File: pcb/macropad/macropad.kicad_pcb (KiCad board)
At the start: 2 copper layers, 100 x 100 mm, 21 parts, among them SW1 SW_Push, SW10 RotaryEncoder, SW2 SW_Push, SW3 SW_Push, SW4 SW_Push, SW5 SW_Push, SW6 SW_Push, SW7 SW_Push, SW8 SW_Push, SW9 SW_Push, U1 XIAO-RP2040-DIP

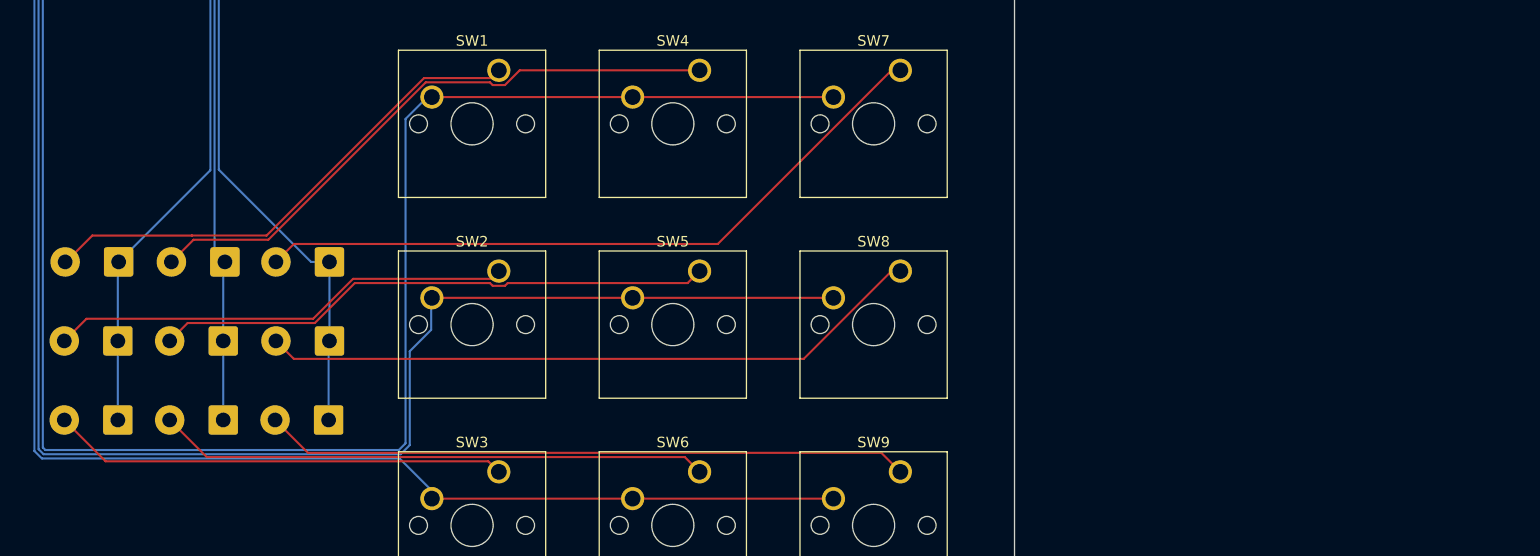
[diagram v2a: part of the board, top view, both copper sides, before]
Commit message: tidy wiring
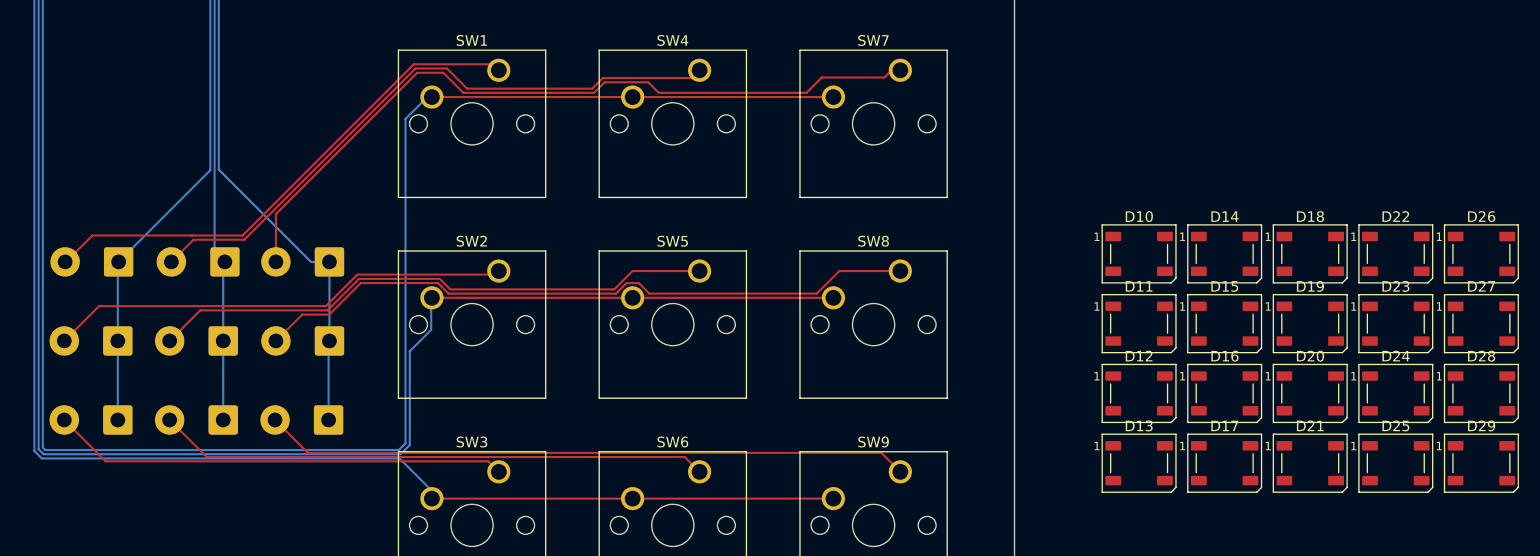
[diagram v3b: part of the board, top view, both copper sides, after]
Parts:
- added D10: WS2812B, LED_SMD:LED_WS2812B_PLCC4_5.0x5.0mm_P3.2mm, F.Cu at (213.8, 104.7)
- added D11: WS2812B, LED_SMD:LED_WS2812B_PLCC4_5.0x5.0mm_P3.2mm, F.Cu at (213.8, 111.4)
- added D12: WS2812B, LED_SMD:LED_WS2812B_PLCC4_5.0x5.0mm_P3.2mm, F.Cu at (213.8, 118.0)
- added D13: WS2812B, LED_SMD:LED_WS2812B_PLCC4_5.0x5.0mm_P3.2mm, F.Cu at (213.8, 124.6)
- added D14: WS2812B, LED_SMD:LED_WS2812B_PLCC4_5.0x5.0mm_P3.2mm, F.Cu at (221.9, 104.7)
- added D15: WS2812B, LED_SMD:LED_WS2812B_PLCC4_5.0x5.0mm_P3.2mm, F.Cu at (221.9, 111.4)
- added D16: WS2812B, LED_SMD:LED_WS2812B_PLCC4_5.0x5.0mm_P3.2mm, F.Cu at (221.9, 118.0)
- added D17: WS2812B, LED_SMD:LED_WS2812B_PLCC4_5.0x5.0mm_P3.2mm, F.Cu at (221.9, 124.6)
- added D18: WS2812B, LED_SMD:LED_WS2812B_PLCC4_5.0x5.0mm_P3.2mm, F.Cu at (230.1, 104.7)
- added D19: WS2812B, LED_SMD:LED_WS2812B_PLCC4_5.0x5.0mm_P3.2mm, F.Cu at (230.1, 111.4)
- added D20: WS2812B, LED_SMD:LED_WS2812B_PLCC4_5.0x5.0mm_P3.2mm, F.Cu at (230.1, 118.0)
- added D21: WS2812B, LED_SMD:LED_WS2812B_PLCC4_5.0x5.0mm_P3.2mm, F.Cu at (230.1, 124.6)
- added D22: WS2812B, LED_SMD:LED_WS2812B_PLCC4_5.0x5.0mm_P3.2mm, F.Cu at (238.2, 104.7)
- added D23: WS2812B, LED_SMD:LED_WS2812B_PLCC4_5.0x5.0mm_P3.2mm, F.Cu at (238.2, 111.4)
- added D24: WS2812B, LED_SMD:LED_WS2812B_PLCC4_5.0x5.0mm_P3.2mm, F.Cu at (238.2, 118.0)
- added D25: WS2812B, LED_SMD:LED_WS2812B_PLCC4_5.0x5.0mm_P3.2mm, F.Cu at (238.2, 124.6)
- added D26: WS2812B, LED_SMD:LED_WS2812B_PLCC4_5.0x5.0mm_P3.2mm, F.Cu at (246.3, 104.7)
- added D27: WS2812B, LED_SMD:LED_WS2812B_PLCC4_5.0x5.0mm_P3.2mm, F.Cu at (246.3, 111.4)
- added D28: WS2812B, LED_SMD:LED_WS2812B_PLCC4_5.0x5.0mm_P3.2mm, F.Cu at (246.3, 118.0)
- added D29: WS2812B, LED_SMD:LED_WS2812B_PLCC4_5.0x5.0mm_P3.2mm, F.Cu at (246.3, 124.6)
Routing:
- net Net-(D7-A): track 65.9 -> 71.0 mm
- net Net-(D4-A): track 57.9 -> 59.2 mm
- net Net-(D5-A): track 53.2 -> 53.9 mm

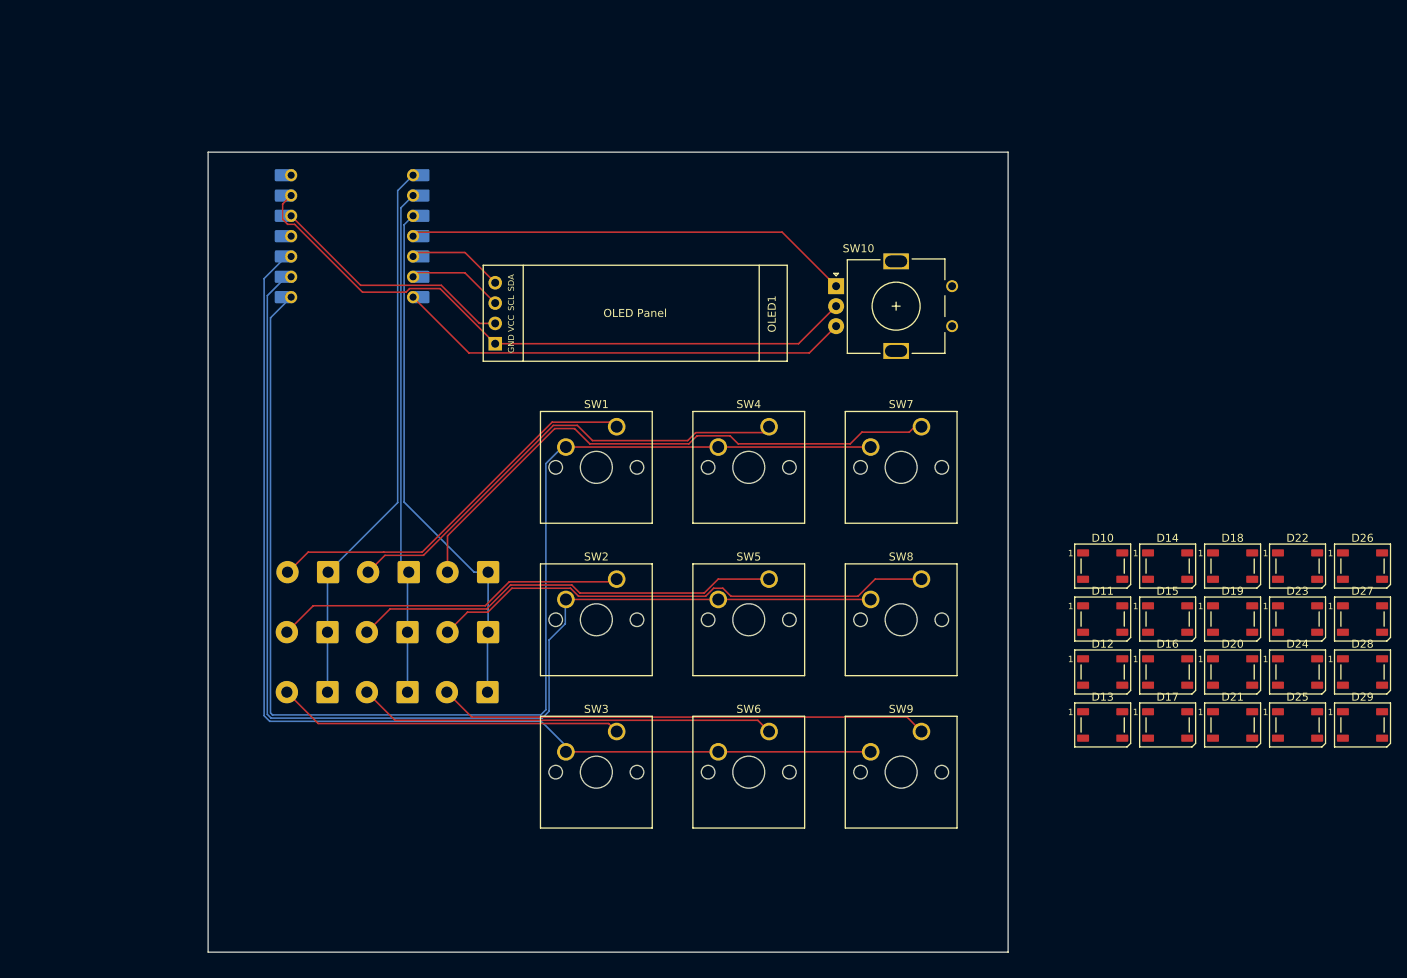
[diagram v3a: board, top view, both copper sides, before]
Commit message: added leds
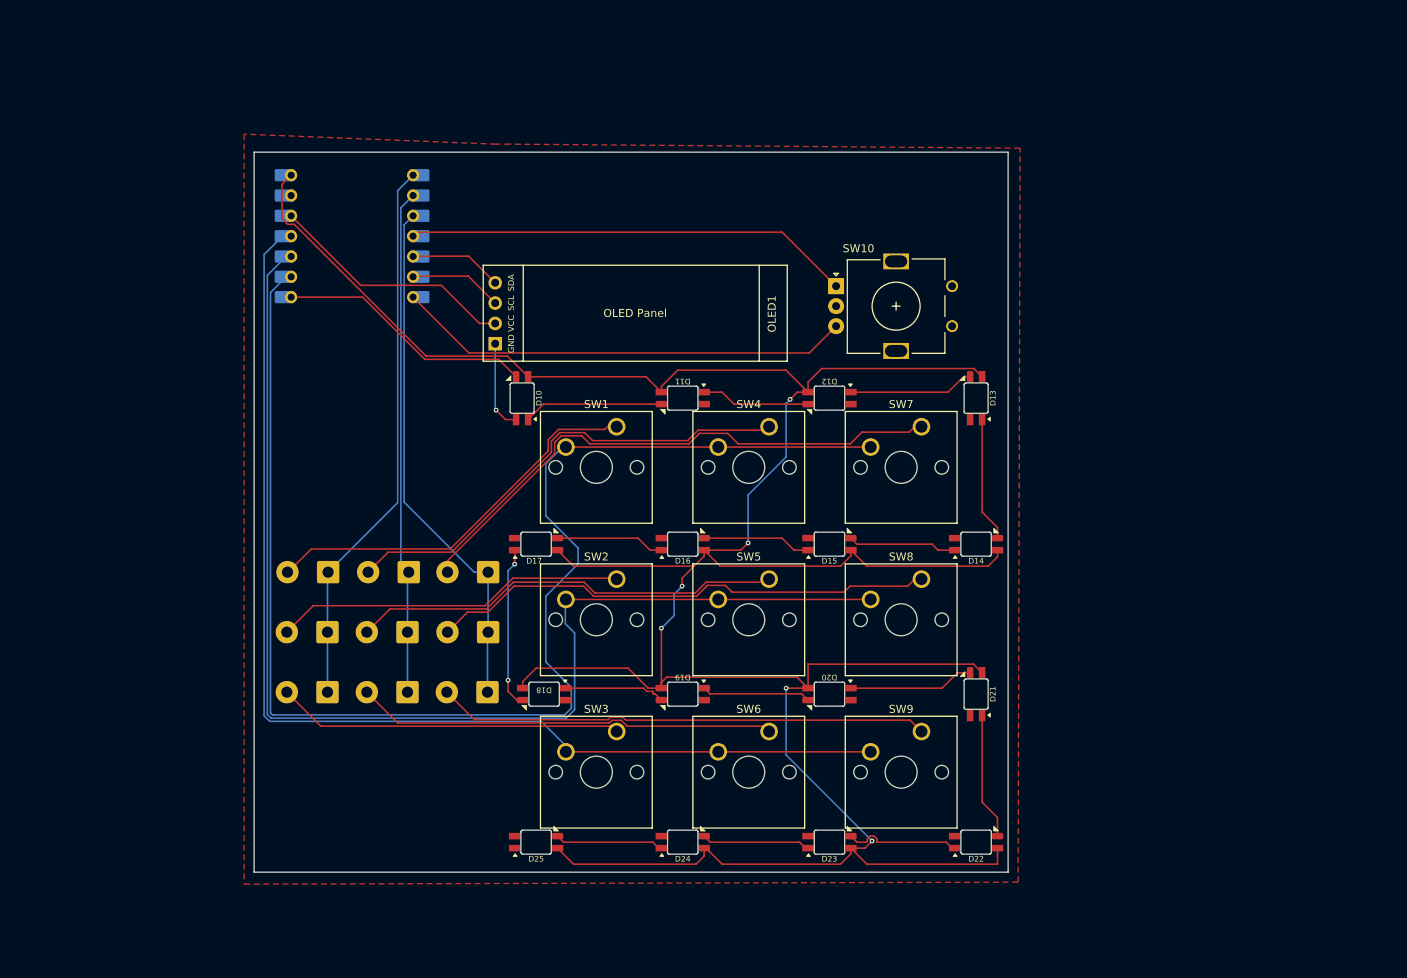
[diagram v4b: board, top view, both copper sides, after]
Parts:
- removed D26, D27, D28, D29: WS2812B, LED_SMD:LED_WS2812B_PLCC4_5.0x5.0mm_P3.2mm
- D10, D11, D12, D13, D14, D15, D16, D17, D18, D19, D20, D21, D22, D23, D24, D25: value WS2812B -> SK6812MINI; footprint LED_SMD:LED_WS2812B_PLCC4_5.0x5.0mm_P3.2mm -> Downloads:SK6812-MINI-E
- moved D25 96.3 mm to (143.0, 139.2)
- moved D18 87.5 mm to (144.0, 120.8), turned to 180 degrees
- moved D17 82.1 mm to (143.0, 102.0)
- moved D24 79.7 mm to (161.3, 139.2)
- moved D10 75.5 mm to (141.2, 83.8), turned to 90 degrees
- moved D19 69.4 mm to (161.3, 120.8), turned to 180 degrees
- moved D23 64.8 mm to (179.7, 139.2)
- moved D16 62.7 mm to (161.3, 102.0)
- moved D11 59.3 mm to (161.3, 83.8), turned to 180 degrees
- moved D22 53.0 mm to (198.0, 139.2)
- moved D20 50.5 mm to (179.7, 120.8), turned to 180 degrees
- moved D12 48.4 mm to (179.7, 83.8), turned to 180 degrees
- moved D13 43.8 mm to (198.0, 83.8), turned to 90 degrees
- moved D15 43.3 mm to (179.7, 102.0)
- moved D21 32.3 mm to (198.0, 120.8), turned to 90 degrees
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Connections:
- D10 pad 1: VCC -> Net-(D10-DOUT)
- D10 pad 2: Net-(D10-DOUT) -> GND
- D10 pad 3: GND -> LED_CNTRL
- D10 pad 4: LED_CNTRL -> VCC
- D11 pad 1: VCC -> Net-(D11-DOUT)
- D11 pad 2: Net-(D11-DOUT) -> GND
- D11 pad 3: GND -> Net-(D10-DOUT)
- D11 pad 4: Net-(D10-DOUT) -> VCC
- D12 pad 1: VCC -> Net-(D12-DOUT)
- D12 pad 2: Net-(D12-DOUT) -> GND
- D12 pad 3: GND -> Net-(D11-DOUT)
- D12 pad 4: Net-(D11-DOUT) -> VCC
- D13 pad 1: VCC -> Net-(D13-DOUT)
- D13 pad 2: Net-(D13-DOUT) -> GND
- D13 pad 3: GND -> Net-(D12-DOUT)
- D13 pad 4: Net-(D12-DOUT) -> VCC
- D14 pad 1: VCC -> Net-(D14-DOUT)
- D14 pad 2: Net-(D14-DOUT) -> GND
- D14 pad 3: GND -> Net-(D13-DOUT)
- D14 pad 4: Net-(D13-DOUT) -> VCC
- D15 pad 1: VCC -> Net-(D15-DOUT)
- D15 pad 2: Net-(D15-DOUT) -> GND
- D15 pad 3: GND -> Net-(D14-DOUT)
- D15 pad 4: Net-(D14-DOUT) -> VCC
- D16 pad 1: VCC -> Net-(D16-DOUT)
- D16 pad 2: Net-(D16-DOUT) -> GND
- D16 pad 3: GND -> Net-(D15-DOUT)
- D16 pad 4: Net-(D15-DOUT) -> VCC
- D17 pad 1: VCC -> Net-(D17-DOUT)
- D17 pad 2: Net-(D17-DOUT) -> GND
- D17 pad 3: GND -> Net-(D16-DOUT)
- D17 pad 4: Net-(D16-DOUT) -> VCC
- D18 pad 1: VCC -> Net-(D18-DOUT)
- D18 pad 2: Net-(D18-DOUT) -> GND
- D18 pad 3: GND -> Net-(D17-DOUT)
- D18 pad 4: Net-(D17-DOUT) -> VCC
- D19 pad 1: VCC -> Net-(D19-DOUT)
- D19 pad 2: Net-(D19-DOUT) -> GND
- D19 pad 3: GND -> Net-(D18-DOUT)
- D19 pad 4: Net-(D18-DOUT) -> VCC
- D20 pad 1: VCC -> Net-(D20-DOUT)
- D20 pad 2: Net-(D20-DOUT) -> GND
- D20 pad 3: GND -> Net-(D19-DOUT)
- D20 pad 4: Net-(D19-DOUT) -> VCC
- D21 pad 1: VCC -> Net-(D21-DOUT)
- D21 pad 2: Net-(D21-DOUT) -> GND
- D21 pad 3: GND -> Net-(D20-DOUT)
- D21 pad 4: Net-(D20-DOUT) -> VCC
- D22 pad 1: VCC -> Net-(D22-DOUT)
- D22 pad 2: Net-(D22-DOUT) -> GND
- D22 pad 3: GND -> Net-(D21-DOUT)
- D22 pad 4: Net-(D21-DOUT) -> VCC
- D23 pad 1: VCC -> Net-(D23-DOUT)
- D23 pad 2: Net-(D23-DOUT) -> GND
- D23 pad 3: GND -> Net-(D22-DOUT)
- D23 pad 4: Net-(D22-DOUT) -> VCC
- D24 pad 1: VCC -> Net-(D24-DOUT)
- D24 pad 2: Net-(D24-DOUT) -> GND
- D24 pad 3: GND -> Net-(D23-DOUT)
- D24 pad 4: Net-(D23-DOUT) -> VCC
- D25 pad 1: VCC -> unconnected-(D25-DOUT-Pad1)
- D25 pad 2: Net-(D25-DOUT) -> GND
- D25 pad 3: GND -> Net-(D24-DOUT)
- D25 pad 4: Net-(D24-DOUT) -> VCC
- U1 pad 10: COL0 -> COL1
- U1 pad 11: LED_CNTRL -> COL0
- U1 pad 8: COL2 -> LED_CNTRL
- U1 pad 9: COL1 -> COL2
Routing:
- net VCC: track 0.00 -> 370.5 mm, vias 0 -> 6
- net GND: track 81.4 -> 11.3 mm, vias 0 -> 1
- net LED_CNTRL: track 0.00 -> 32.2 mm
- net Net-(D17-DOUT): track 0.00 -> 20.3 mm, vias 0 -> 2
- net Net-(D10-DOUT): track 0.00 -> 17.3 mm
- net Net-(D21-DOUT): track 0.00 -> 15.9 mm
- net Net-(D20-DOUT): track 0.00 -> 15.7 mm
- net Net-(D12-DOUT): track 0.00 -> 15.7 mm
- net Net-(D13-DOUT): track 0.00 -> 15.6 mm
- net Net-(D22-DOUT): track 0.00 -> 14.3 mm
- net Net-(D15-DOUT): track 0.00 -> 13.6 mm
- net Net-(D11-DOUT): track 0.00 -> 13.6 mm
- net Net-(D19-DOUT): track 0.00 -> 13.6 mm
- net Net-(D16-DOUT): track 0.00 -> 13.6 mm
- net Net-(D14-DOUT): track 0.00 -> 13.6 mm
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- added copper zone on F.Cu, net GND
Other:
- board size 100 x 100 mm -> 94.2 x 90 mm

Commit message: added the ec11 as a switch and some extra organization
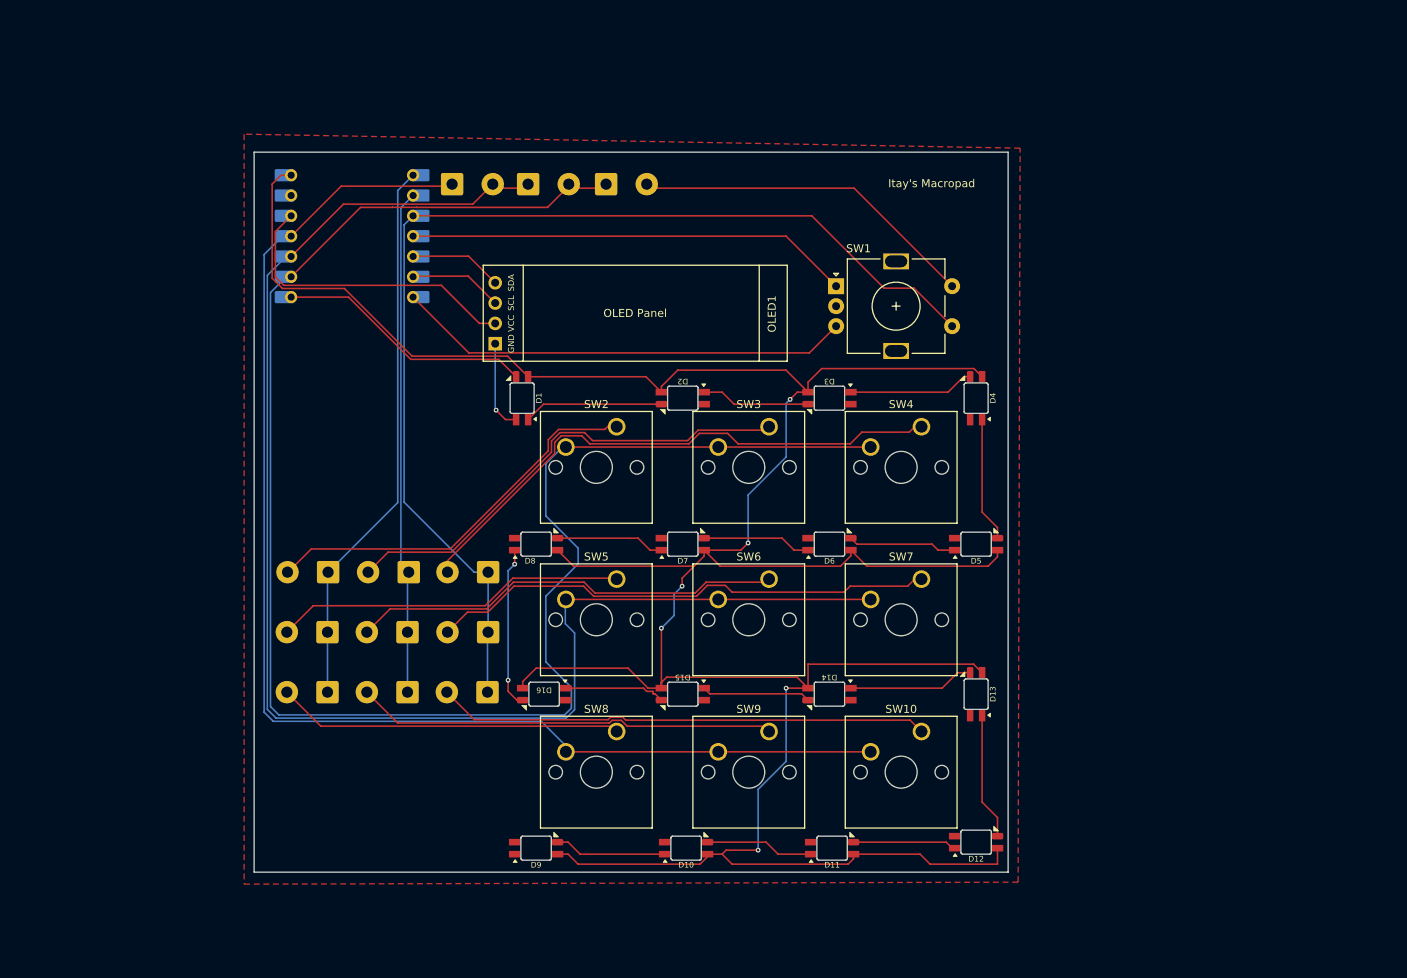
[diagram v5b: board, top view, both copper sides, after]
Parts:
- added D17: D_Small, Diode_THT:D_5W_P5.08mm_Vertical_AnodeUp, B.Cu at (151.8, 57.0)
- added D18: D_Small, Diode_THT:D_5W_P5.08mm_Vertical_AnodeUp, B.Cu at (142.0, 57.0)
- added D19: D_Small, Diode_THT:D_5W_P5.08mm_Vertical_AnodeUp, B.Cu at (132.5, 57.0)
- SW1: renamed from SW10; footprint Downloads:RotaryEncoder_Alps_EC11E_Vertical_H20mm -> Rotary_Encoder:RotaryEncoder_Alps_EC11E-Switch_Vertical_H20mm
- moved D10 0.86 mm to (161.8, 140.0)
- moved D11 0.82 mm to (180.0, 140.0)
- moved D9 0.75 mm to (143.0, 140.0)
- renumbered D10 to D1, D24 to D10, D23 to D11, D22 to D12, D21 to D13, D20 to D14, D19 to D15, D18 to D16, D11 to D2, D7 to D20, D4 to D21, D1 to D22, D8 to D23, D5 to D24, D2 to D25, D9 to D26, D6 to D27, D3 to D28, D12 to D3, D13 to D4, D14 to D5, D15 to D6, D16 to D7, D17 to D8, D25 to D9, SW9 to SW10, SW1 to SW2, SW4 to SW3, SW7 to SW4, SW2 to SW5, SW5 to SW6, SW8 to SW7, SW3 to SW8, SW6 to SW9
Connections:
- D20 pad 1: ROW2 -> EC11_S1
- D23 pad 1: ROW2 -> EC11_S1
- D26 pad 1: ROW2 -> EC11_S1
- U1 pad 3: ROW2 -> EC11_S1
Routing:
- net EC11_S1: track 0.00 -> 138.4 mm
- net ROW2: track 65.3 -> 0.00 mm
- net COL2: track 169.7 -> 212.8 mm
- net EC11_S2: track 0.00 -> 43.0 mm
- net COL1: track 149.5 -> 181.8 mm
- net COL0: track 138.3 -> 160.5 mm
- net VCCQ: track 31.1 -> 38.3 mm
- net VCC: track 370.5 -> 375.4 mm
- net Net-(D11-DIN): track 14.3 -> 12.6 mm
- net Net-(D10-DOUT): track 13.3 -> 14.0 mm
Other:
- board text added: "Itay's Macropad"
- board text added: "XIAO HERE"
